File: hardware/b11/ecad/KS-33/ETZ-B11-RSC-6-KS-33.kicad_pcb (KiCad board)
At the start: 2 copper layers, 131.5 x 85.8 mm, 44 parts, among them SW1 KS-2P02B01-01-a, SW10 KS-2P02B01-01-a, SW11 KS-2P02B01-01-a, SW12 KS-2P02B01-01-a, SW13 KS-2P02B01-01-a, SW14 KS-2P02B01-01-a, SW15 KS-2P02B01-01-a, SW16 KS-2P02B01-01-a, SW17 KS-2P02B01-01-a, SW18 KS-2P02B01-01-a, SW19 KS-2P02B01-01-a, SW2 KS-2P02B01-01-a, SW20 KS-2P02B01-01-a, SW21 KS-2P02B01-01-a, SW22 KS-2P02B01-01-a, SW3 KS-2P02B01-01-a, SW4 KS-2P02B01-01-a, SW5 KS-2P02B01-01-a, SW6 KS-2P02B01-01-a, SW7 KS-2P02B01-01-a, SW8 KS-2P02B01-01-a, SW9 KS-2P02B01-01-a

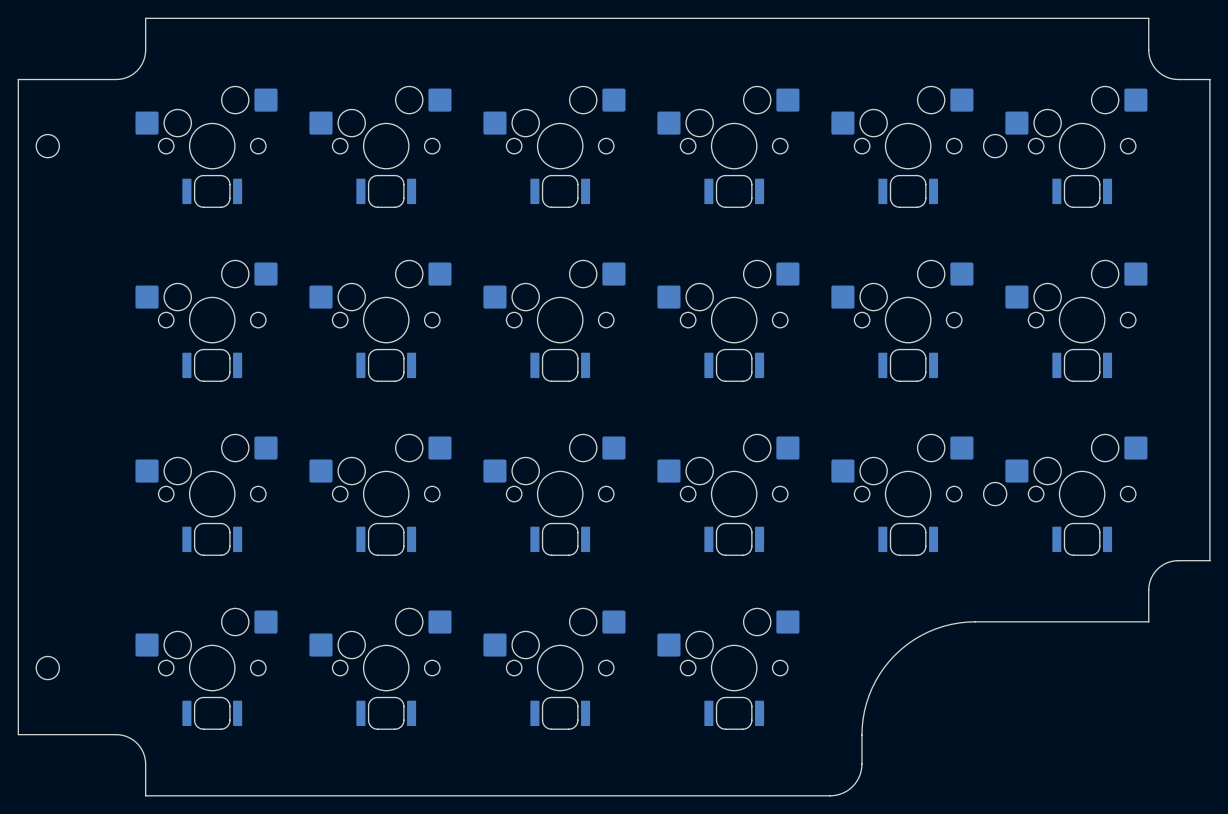
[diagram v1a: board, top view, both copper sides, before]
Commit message: feat: add B11 switch plate schematic foundation (#58)
Signed-off-by: Nikola Secerovski <secersh@gmail.com>
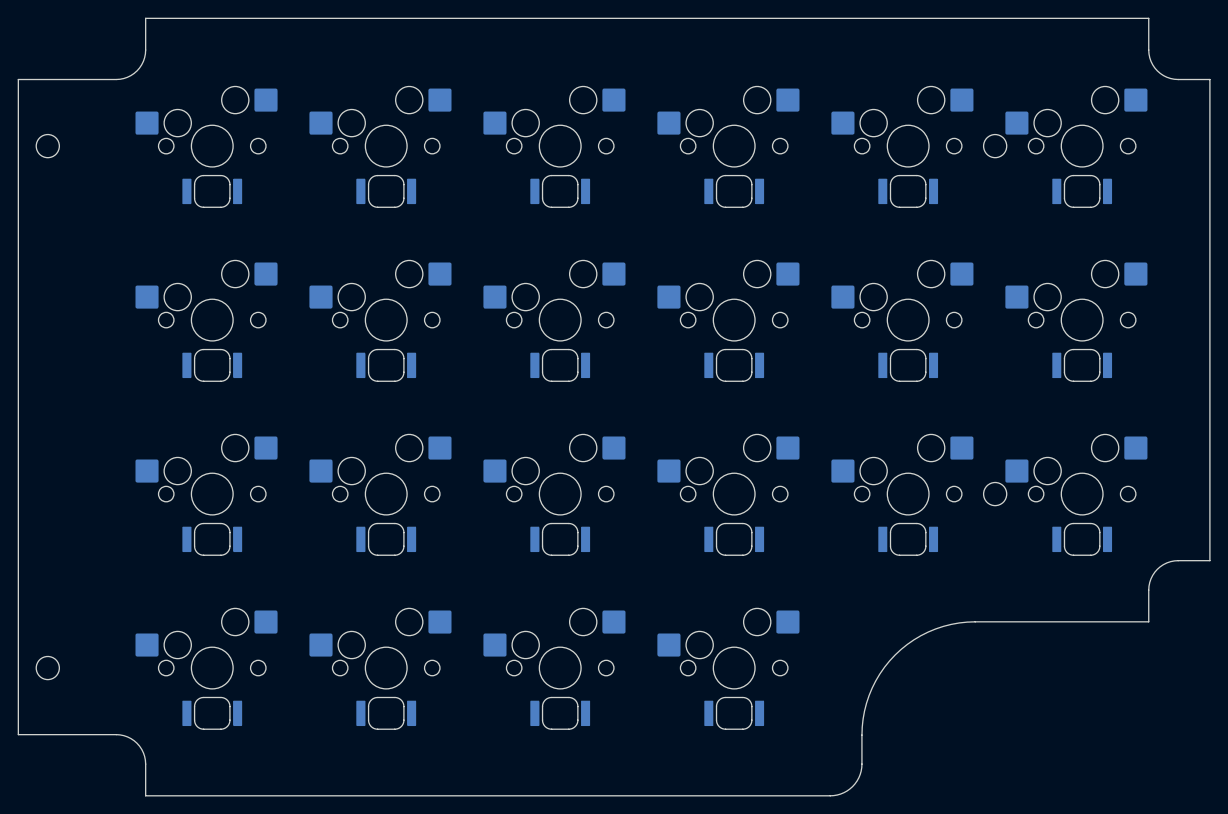
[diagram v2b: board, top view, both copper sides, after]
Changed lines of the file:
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@@
 		(pad "" np_thru_hole circle
 			(at 0 0)
-			(size 5 5)
-			(drill 5)
+			(size 4.6 4.6)
+			(drill 4.6)
 			(layers "*.Cu" "*.Mask")
 		)
@@
 		(pad "" np_thru_hole circle
 			(at 0 0)
-			(size 5 5)
-			(drill 5)
+			(size 4.6 4.6)
+			(drill 4.6)
 			(layers "*.Cu" "*.Mask")
 		)
@@
 		(pad "" np_thru_hole circle
 			(at 0 0)
-			(size 5 5)
-			(drill 5)
+			(size 4.6 4.6)
+			(drill 4.6)
 			(layers "*.Cu" "*.Mask")
 		)
@@
 		(pad "" np_thru_hole circle
 			(at 0 0)
-			(size 5 5)
-			(drill 5)
+			(size 4.6 4.6)
+			(drill 4.6)
 			(layers "*.Cu" "*.Mask")
 		)
@@
 		(pad "" np_thru_hole circle
 			(at 0 0)
-			(size 5 5)
-			(drill 5)
+			(size 4.6 4.6)
+			(drill 4.6)
 			(layers "*.Cu" "*.Mask")
 		)
@@
 		(pad "" np_thru_hole circle
 			(at 0 0)
-			(size 5 5)
-			(drill 5)
+			(size 4.6 4.6)
+			(drill 4.6)
 			(layers "*.Cu" "*.Mask")
 		)
@@
 		(pad "" np_thru_hole circle
 			(at 0 0)
-			(size 5 5)
-			(drill 5)
+			(size 4.6 4.6)
+			(drill 4.6)
 			(layers "*.Cu" "*.Mask")
 		)
@@
 		(pad "" np_thru_hole circle
 			(at 0 0)
-			(size 5 5)
-			(drill 5)
+			(size 4.6 4.6)
+			(drill 4.6)
 			(layers "*.Cu" "*.Mask")
 		)
@@
 		(pad "" np_thru_hole circle
 			(at 0 0)
-			(size 5 5)
-			(drill 5)
+			(size 4.6 4.6)
+			(drill 4.6)
 			(layers "*.Cu" "*.Mask")
 		)
@@
 		(pad "" np_thru_hole circle
 			(at 0 0)
-			(size 5 5)
-			(drill 5)
+			(size 4.6 4.6)
+			(drill 4.6)
 			(layers "*.Cu" "*.Mask")
 		)
@@
 		(pad "" np_thru_hole circle
 			(at 0 0)
-			(size 5 5)
-			(drill 5)
+			(size 4.6 4.6)
+			(drill 4.6)
 			(layers "*.Cu" "*.Mask")
 		)
@@
 		(pad "" np_thru_hole circle
 			(at 0 0)
-			(size 5 5)
-			(drill 5)
+			(size 4.6 4.6)
+			(drill 4.6)
 			(layers "*.Cu" "*.Mask")
 		)
@@
 		(pad "" np_thru_hole circle
 			(at 0 0)
-			(size 5 5)
-			(drill 5)
+			(size 4.6 4.6)
+			(drill 4.6)
 			(layers "*.Cu" "*.Mask")
 		)
@@
 		(pad "" np_thru_hole circle
 			(at 0 0)
-			(size 5 5)
-			(drill 5)
+			(size 4.6 4.6)
+			(drill 4.6)
 			(layers "*.Cu" "*.Mask")
 		)
@@
 		(pad "" np_thru_hole circle
 			(at 0 0)
-			(size 5 5)
-			(drill 5)
+			(size 4.6 4.6)
+			(drill 4.6)
 			(layers "*.Cu" "*.Mask")
 		)
@@
 		(pad "" np_thru_hole circle
 			(at 0 0)
-			(size 5 5)
-			(drill 5)
+			(size 4.6 4.6)
+			(drill 4.6)
 			(layers "*.Cu" "*.Mask")
 		)
@@
 		(pad "" np_thru_hole circle
 			(at 0 0)
-			(size 5 5)
-			(drill 5)
+			(size 4.6 4.6)
+			(drill 4.6)
 			(layers "*.Cu" "*.Mask")
 		)
@@
 		(pad "" np_thru_hole circle
 			(at 0 0)
-			(size 5 5)
-			(drill 5)
+			(size 4.6 4.6)
+			(drill 4.6)
 			(layers "*.Cu" "*.Mask")
 		)
@@
 		(pad "" np_thru_hole circle
 			(at 0 0)
-			(size 5 5)
-			(drill 5)
+			(size 4.6 4.6)
+			(drill 4.6)
 			(layers "*.Cu" "*.Mask")
 		)
@@
 		(pad "" np_thru_hole circle
 			(at 0 0)
-			(size 5 5)
-			(drill 5)
+			(size 4.6 4.6)
+			(drill 4.6)
 			(layers "*.Cu" "*.Mask")
 		)
@@
 		(pad "" np_thru_hole circle
 			(at 0 0)
-			(size 5 5)
-			(drill 5)
+			(size 4.6 4.6)
+			(drill 4.6)
 			(layers "*.Cu" "*.Mask")
 		)
@@
 		(pad "" np_thru_hole circle
 			(at 0 0)
-			(size 5 5)
-			(drill 5)
+			(size 4.6 4.6)
+			(drill 4.6)
 			(layers "*.Cu" "*.Mask")
 		)
